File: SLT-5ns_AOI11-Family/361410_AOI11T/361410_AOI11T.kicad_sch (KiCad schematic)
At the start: 17 parts, among them T1 T_DB, T2 T_DA, U1 12-Pin_SLx_Can

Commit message: Updated schematics
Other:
- note removed: "B"
- note removed: "C"
- note removed: "E"
- note removed: "Transistor Die Layout (top view)"
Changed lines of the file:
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@@
     (stroke (width 0) (type default) (color 0 0 0 0))
-  )
-  (polyline (pts (xy 252.73 29.21) (xy 252.73 40.64))
-    (stroke (width 0) (type solid) (color 0 0 0 0))
   )
   (wire (pts (xy 53.34 93.98) (xy 60.96 93.98))
     (stroke (width 0) (type default) (color 0 0 0 0))
-  )
-  (polyline (pts (xy 264.16 40.64) (xy 252.73 40.64))
-    (stroke (width 0) (type solid) (color 0 0 0 0))
   )
   (wire (pts (xy 138.43 115.57) (xy 147.32 115.57))
@@
   (wire (pts (xy 78.74 80.01) (xy 68.58 80.01))
     (stroke (width 0) (type default) (color 0 0 0 0))
-  )
-  (polyline (pts (xy 252.73 29.21) (xy 264.16 29.21))
-    (stroke (width 0) (type solid) (color 0 0 0 0))
   )
   (wire (pts (xy 95.25 93.98) (xy 91.44 93.98))
@@
   (wire (pts (xy 152.4 93.98) (xy 152.4 105.41))
     (stroke (width 0) (type default) (color 0 0 0 0))
-  )
-  (polyline (pts (xy 264.16 29.21) (xy 264.16 40.64))
-    (stroke (width 0) (type solid) (color 0 0 0 0))
   )
   (wire (pts (xy 139.7 93.98) (xy 152.4 93.98))
@@
     (effects (font (size 1.27 1.27)) (justify left bottom))
   )
-  (text "C" (at 257.81 39.37 0)
-    (effects (font (size 1.27 1.27)) (justify left bottom))
-  )
-  (text "E" (at 254 33.02 0)
-    (effects (font (size 1.27 1.27)) (justify left bottom))
-  )
   (text "(No Noise Rejection)" (at 59.69 119.38 0)
     (effects (font (size 1.27 1.27)) (justify left bottom))
   )
-  (text "B" (at 261.62 33.02 0)
-    (effects (font (size 1.27 1.27)) (justify left bottom))
-  )
-  (text "Transistor Die Layout (top view)" (at 243.84 27.94 0)
-    (effects (font (size 1.27 1.27)) (justify left bottom))
-  )

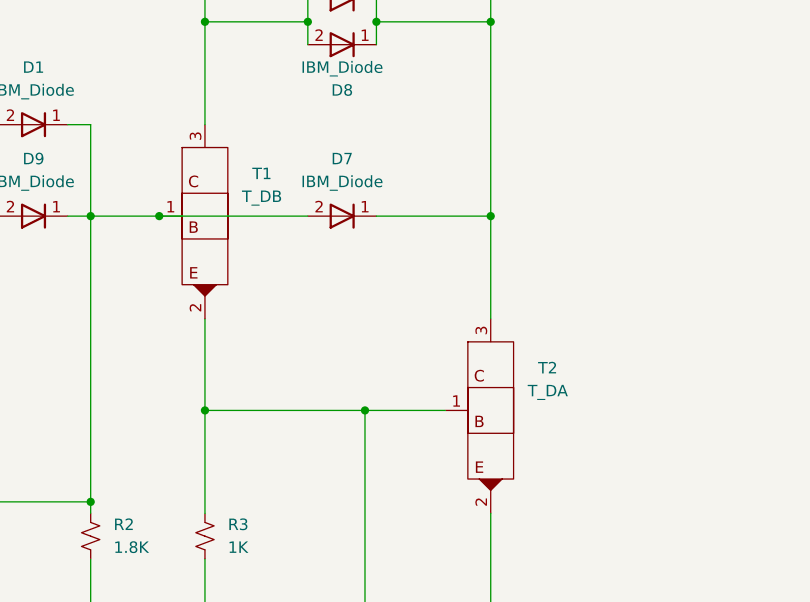
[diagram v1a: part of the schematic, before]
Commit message: Finished off the SLT-30 family of parts, started on the SLT-700 family. Changed labeling of transistors and diodes in all schematics, but have yet to update all the pdf files. This is a TODO...
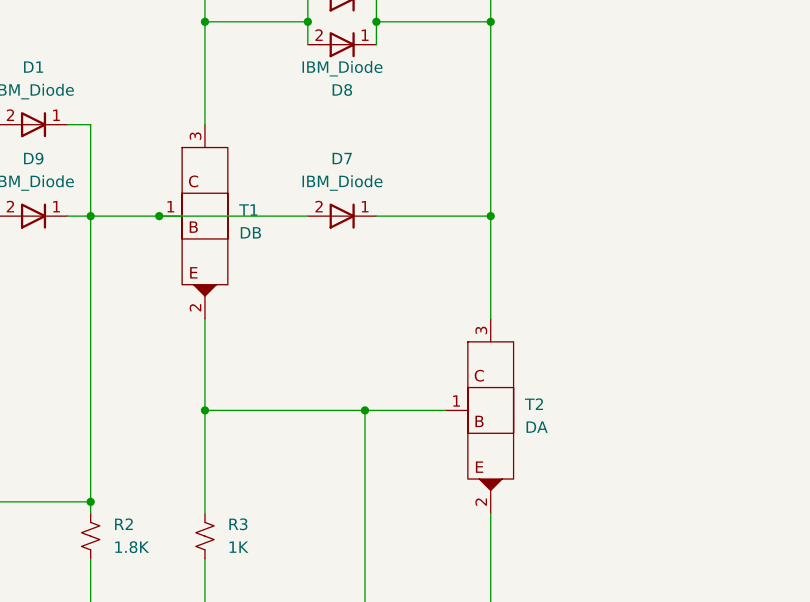
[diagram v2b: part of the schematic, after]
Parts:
- T1: value T_DB -> DB
- T2: value T_DA -> DA
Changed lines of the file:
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@@
   (symbol (lib_id "IBM_SLT-SLD:T_DB") (at 120.65 93.98 0) (unit 1)
     (in_bom yes) (on_board yes) (fields_autoplaced)
-    (property "Reference" "T1" (id 0) (at 127 89.281 0))
-    (property "Value" "T_DB" (id 1) (at 127 91.821 0))
+    (property "Reference" "T1" (id 0) (at 124.46 93.3449 0)
+      (effects (font (size 1.27 1.27)) (justify left))
+    )
+    (property "Value" "DB" (id 1) (at 124.46 95.8849 0)
+      (effects (font (size 1.27 1.27)) (justify left))
+    )
     (property "Footprint" "Package_DFN_QFN:Diodes_DFN1006-3" (id 2) (at 120.65 93.98 0)
       (effects (font (size 1.27 1.27)) hide)
@@
   (symbol (lib_id "IBM_SLT-SLD:T_DA") (at 152.4 115.57 0) (unit 1)
     (in_bom yes) (on_board yes) (fields_autoplaced)
-    (property "Reference" "T2" (id 0) (at 158.75 110.871 0))
-    (property "Value" "T_DA" (id 1) (at 158.75 113.411 0))
+    (property "Reference" "T2" (id 0) (at 156.21 114.9349 0)
+      (effects (font (size 1.27 1.27)) (justify left))
+    )
+    (property "Value" "DA" (id 1) (at 156.21 117.4749 0)
+      (effects (font (size 1.27 1.27)) (justify left))
+    )
     (property "Footprint" "Package_DFN_QFN:Diodes_DFN1006-3" (id 2) (at 152.4 115.57 0)
       (effects (font (size 1.27 1.27)) hide)
@@
     )
     (path "/95303cff-6932-4821-b7e1-1e8ef06881c6"
-      (reference "T1") (unit 1) (value "T_DB") (footprint "Package_DFN_QFN:Diodes_DFN1006-3")
+      (reference "T1") (unit 1) (value "DB") (footprint "Package_DFN_QFN:Diodes_DFN1006-3")
     )
     (path "/aca742d5-d20c-41e7-9ac8-8b36b22cfba4"
-      (reference "T2") (unit 1) (value "T_DA") (footprint "Package_DFN_QFN:Diodes_DFN1006-3")
+      (reference "T2") (unit 1) (value "DA") (footprint "Package_DFN_QFN:Diodes_DFN1006-3")
     )
     (path "/75e072b9-86c1-407b-a1c4-16b7a7044004"
